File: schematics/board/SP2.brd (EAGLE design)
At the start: 30 x 38 mm, 12 parts

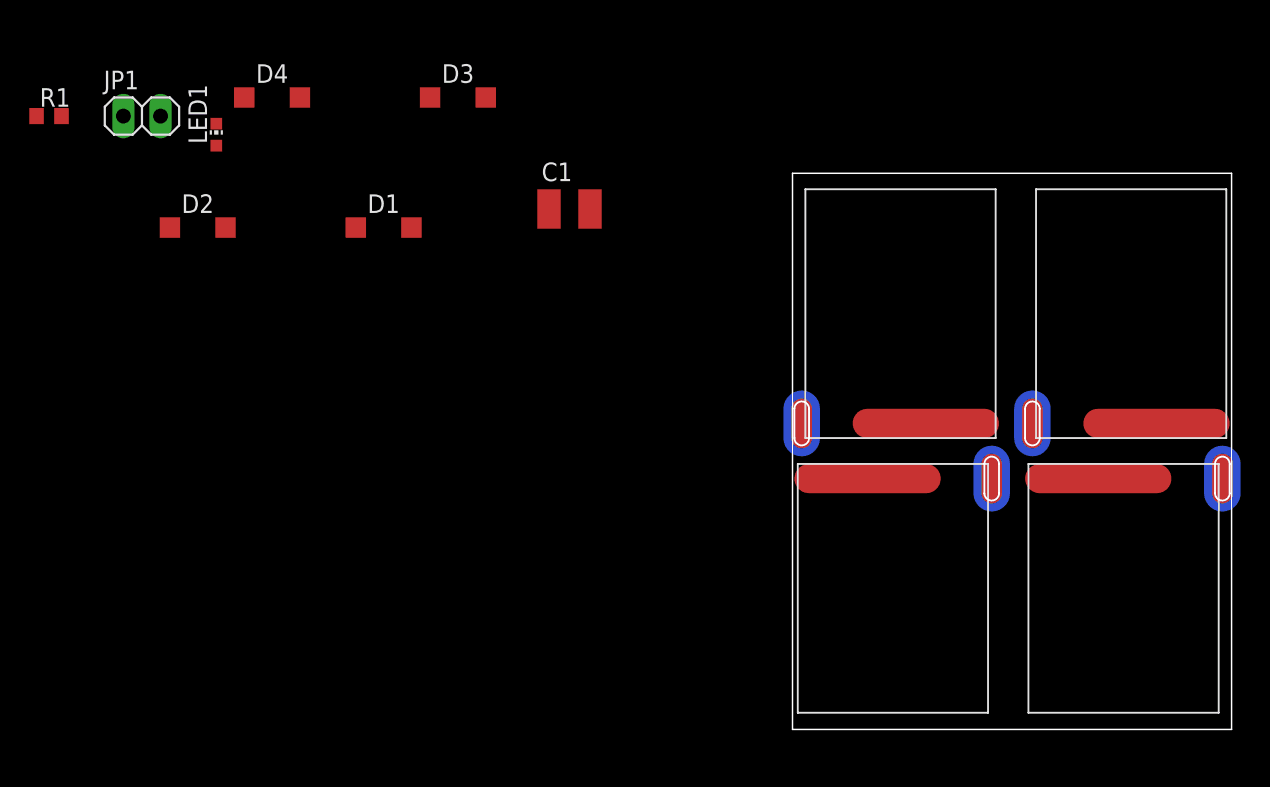
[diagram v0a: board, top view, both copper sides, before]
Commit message: развёл плату солнечных панелей(на деньги)
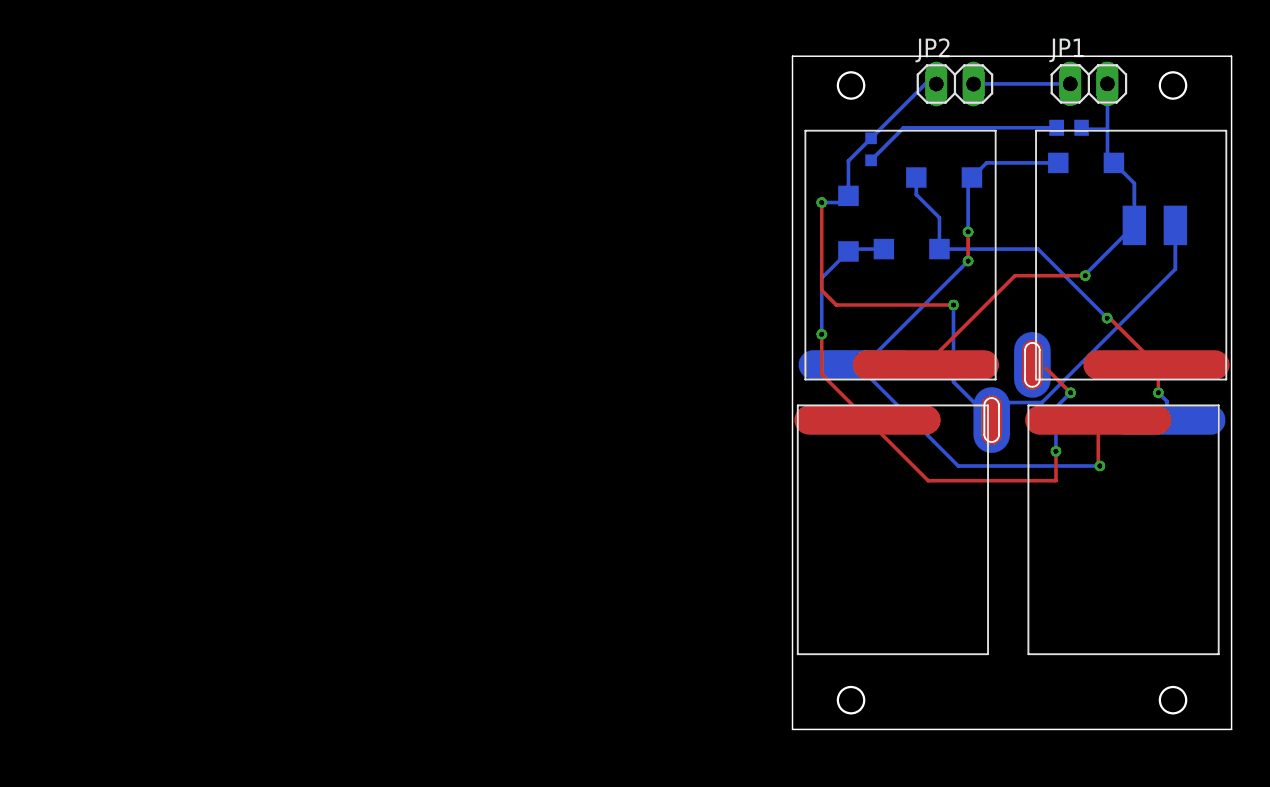
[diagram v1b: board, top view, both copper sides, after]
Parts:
- added JP2: (no value), pinhead:1X02
- U$1, U$2: value SOLAR-2_0 -> SOLAR-2_1; device CanCubeSat:SOLAR_0-2 -> CanCubeSat:SOLAR_1-2
- moved R1 69.7 mm to (18.9, 41.1), flipped to the bottom
- moved JP1 64.7 mm to (20.2, 44.1)
- moved D2 51.1 mm to (10.4, 37.7), flipped to the bottom, turned to 180 degrees
- moved D1 48.2 mm to (20.1, 38.7), flipped to the bottom, turned to 180 degrees
- moved LED1 44.8 mm to (5.37, 39.6), flipped to the bottom
- moved D4 40.3 mm to (3.82, 34.6), flipped to the bottom, turned to 270 degrees
- moved C1 40.0 mm to (24.8, 34.4), flipped to the bottom, turned to 180 degrees
- moved D3 32.7 mm to (8.14, 32.8), flipped to the bottom, turned to 180 degrees
- moved U$2 4.00 mm to (22.6, 13.6)
- moved U$4 4.00 mm to (6.86, 13.6)
- moved U$1 4.00 mm to (7.38, 32.4)
- moved U$3 4.00 mm to (23.1, 32.4)
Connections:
- new net SP+-: C1.2, D4.C, JP2.1, LED1.C, U$4.OUT-2, U$4.OUT-21
- net N$1: now also U$1.OUT; no longer U$1.OUT-2, U$1.OUT-21
- net N$2: now also U$2.OUT; no longer U$2.OUT-2, U$2.OUT-21
- net SP-: now also JP2.2; no longer C1.2, D4.C, LED1.C, U$4.OUT-2, U$4.OUT-21
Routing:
- net SP+-: track 0.00 -> 54.1 mm, vias 0 -> 2
- net N$1: track 0.00 -> 45.3 mm, vias 0 -> 3
- net N$3: track 0.00 -> 39.4 mm, vias 0 -> 3
- net SP+: track 0.00 -> 31.7 mm, vias 0 -> 1
- net N$2: track 0.00 -> 27.7 mm, vias 0 -> 2
- net N$4: track 0.00 -> 13.6 mm
- net SP-: track 0.00 -> 6.61 mm
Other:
- board size 30 x 38 mm -> 30 x 46 mm

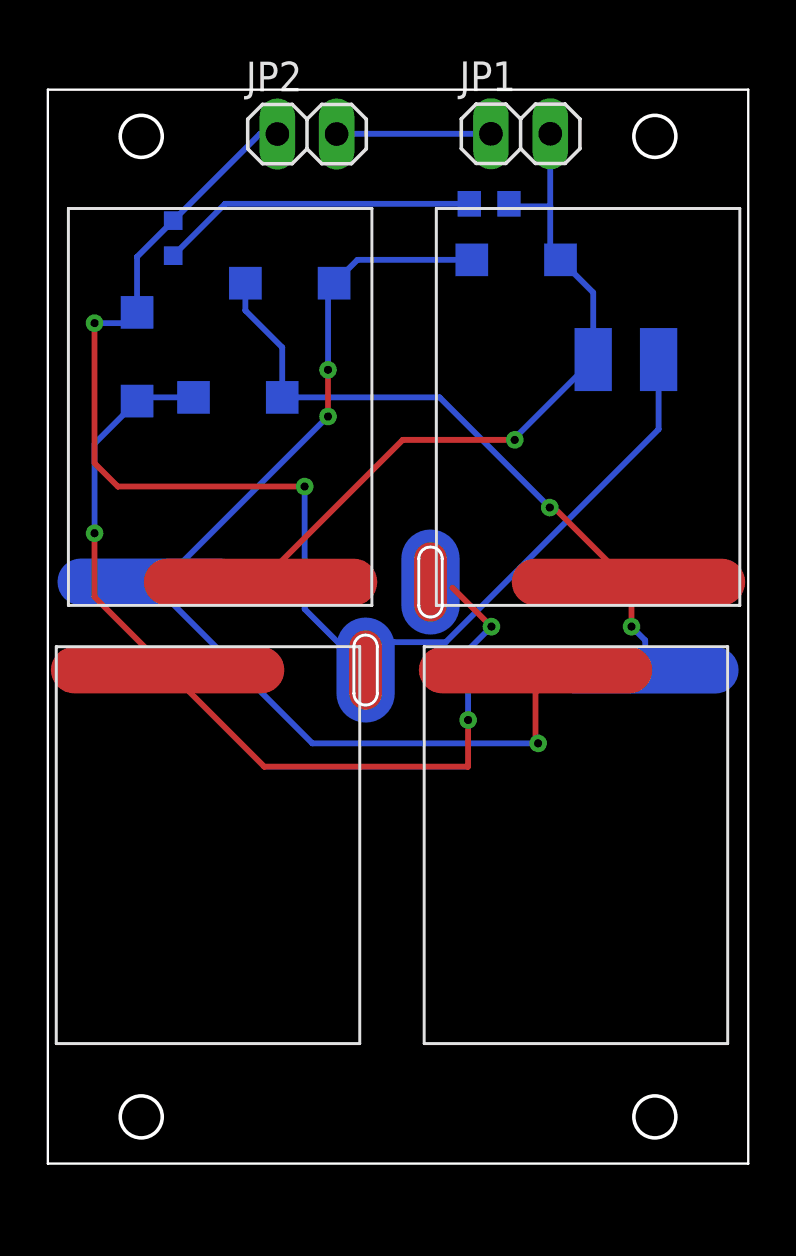
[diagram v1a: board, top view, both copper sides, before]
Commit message: Добавлена плата мотора в сборку
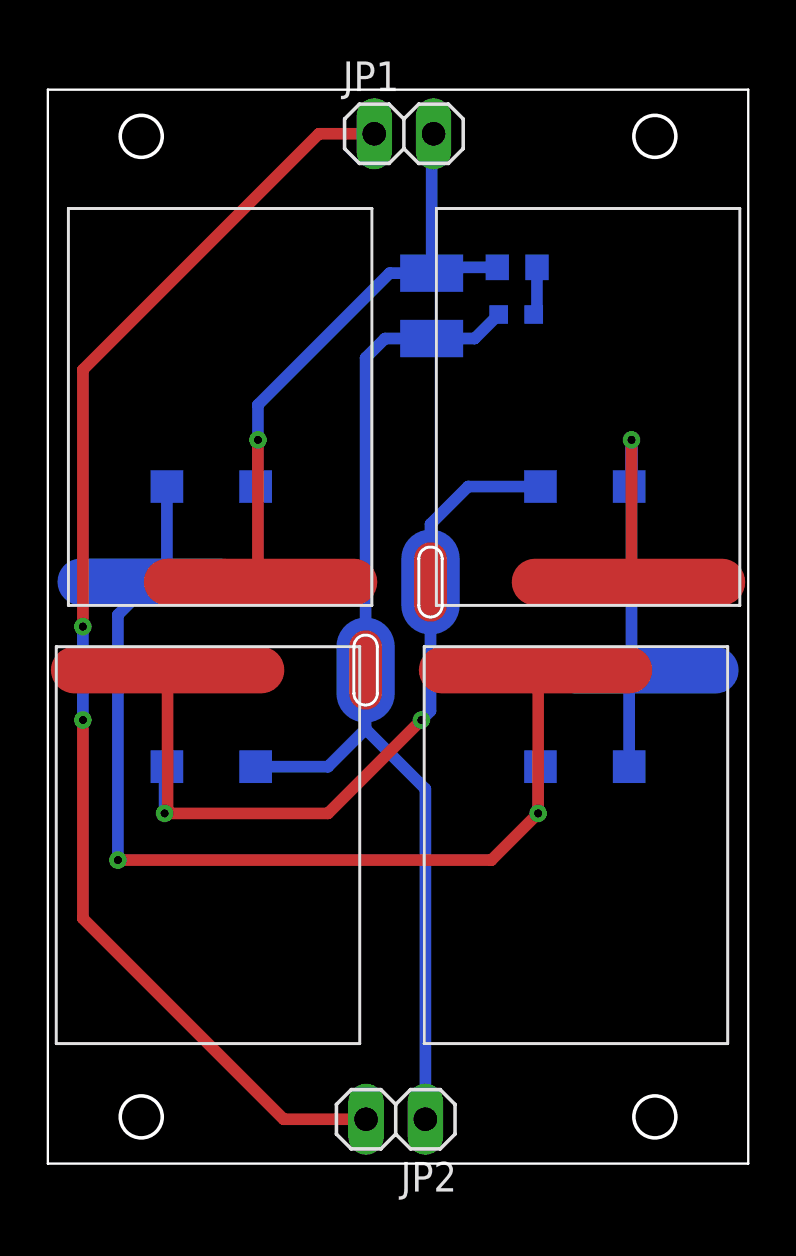
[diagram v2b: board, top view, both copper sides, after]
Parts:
- moved JP2 42.4 mm to (14.9, 1.90), turned to 180 degrees
- moved D2 24.3 mm to (23.0, 17.0), turned to 0 degrees
- moved D4 17.8 mm to (7.00, 17.0), turned to 0 degrees
- moved D1 16.3 mm to (7.00, 29.0)
- moved D3 15.3 mm to (23.0, 29.0)
- moved LED1 15.0 mm to (20.1, 36.4), turned to 270 degrees
- moved C1 8.63 mm to (16.4, 36.7), turned to 270 degrees
- moved JP1 5.00 mm to (15.2, 44.1)
- moved R1 2.97 mm to (20.1, 38.4), turned to 180 degrees
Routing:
- net SP-: track 6.61 -> 55.9 mm, vias 0 -> 2
- net N$4: track 13.6 -> 2.08 mm
- net SP+-: track 54.1 -> 45.5 mm, vias 2 -> 0
- net N$2: track 27.7 -> 22.7 mm, vias 2 -> 1
- net N$3: track 39.4 -> 34.8 mm, vias 3 -> 2
- net SP+: track 31.7 -> 28.8 mm
- net N$1: track 45.3 -> 43.9 mm, vias 3 -> 2

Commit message: Подготовлены платы SP и mtr
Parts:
- added FOTO: VT93N1VERT, KNPN-2023:VT93N1-VERT
- added U$7: (no value), KNPN-2023:VIAS-CONNECT
- U$1, U$2: device CanCubeSat:SOLAR_1-2 -> KNPN-2023:SOLAR_1-2
- U$3, U$4: device CanCubeSat:SOLAR_0-2 -> KNPN-2023:SOLAR_0-2
- moved JP1 1.39 mm to (14.0, 43.5)
- moved U$4 0.37 mm to (7.20, 13.5)
- moved U$3 0.35 mm to (22.8, 32.5)
- moved U$2 0.23 mm to (22.8, 13.5)
- moved U$1 0.20 mm to (7.20, 32.5)
- renumbered JP2 to SP-OUT, LED1 to PWR
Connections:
- net SP+-: now also U$7.1
- net SP-: now also U$7.2
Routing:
- net SP+-: track 45.5 -> 57.0 mm, vias 0 -> 1
- net SP+: track 28.8 -> 36.6 mm
- net N$2: track 22.7 -> 15.0 mm
- net N$3: track 34.8 -> 39.9 mm
- net N$1: track 43.9 -> 40.7 mm
- net SP-: track 55.9 -> 56.4 mm
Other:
- board text added: "+"
- board text added: "-"
- board text added: "SPin"
- board text added: "SPout"
